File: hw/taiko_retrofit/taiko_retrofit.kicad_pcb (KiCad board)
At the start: 2 copper layers, 50 x 36 mm, 12 parts, among them J1 Conn_01x02, J2 Conn_01x03, J3 Conn_01x04, J4 Conn_01x02, U1 RP2040-Zero

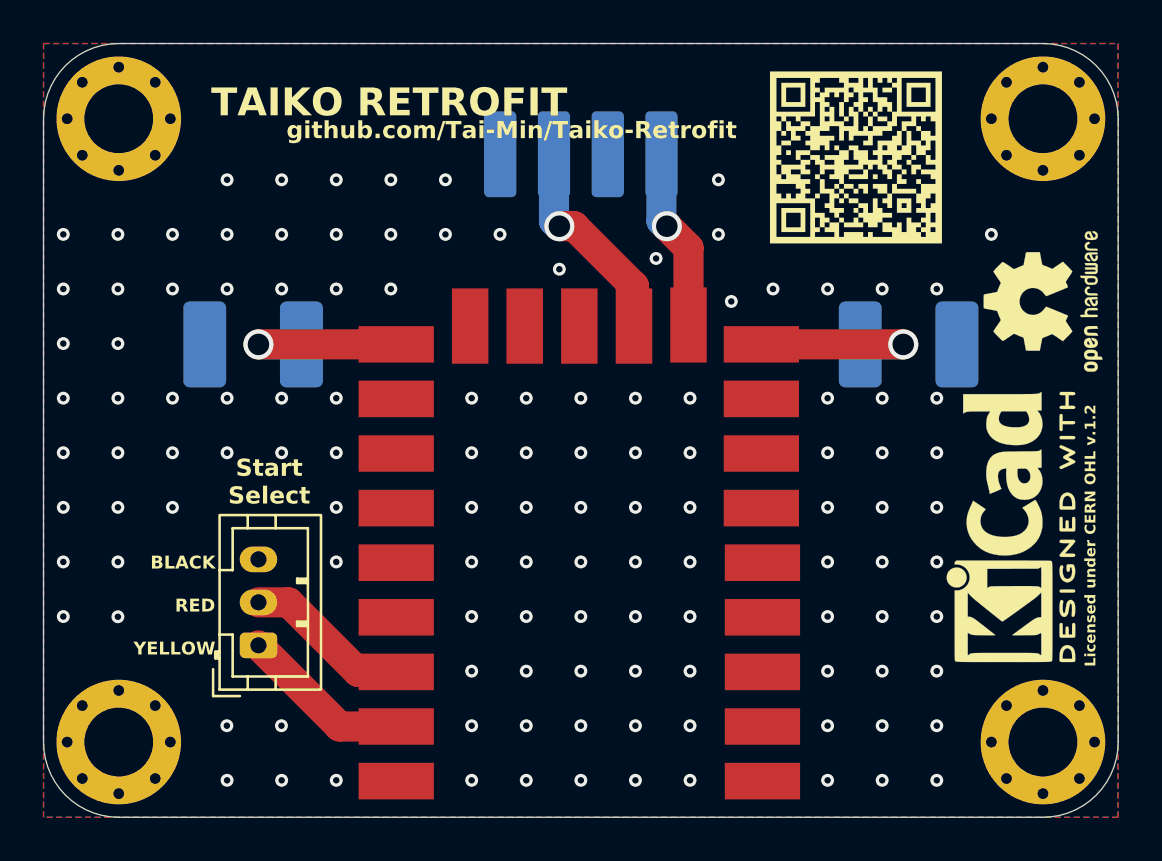
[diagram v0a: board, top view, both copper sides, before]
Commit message: Update PCB layout, add thanks README
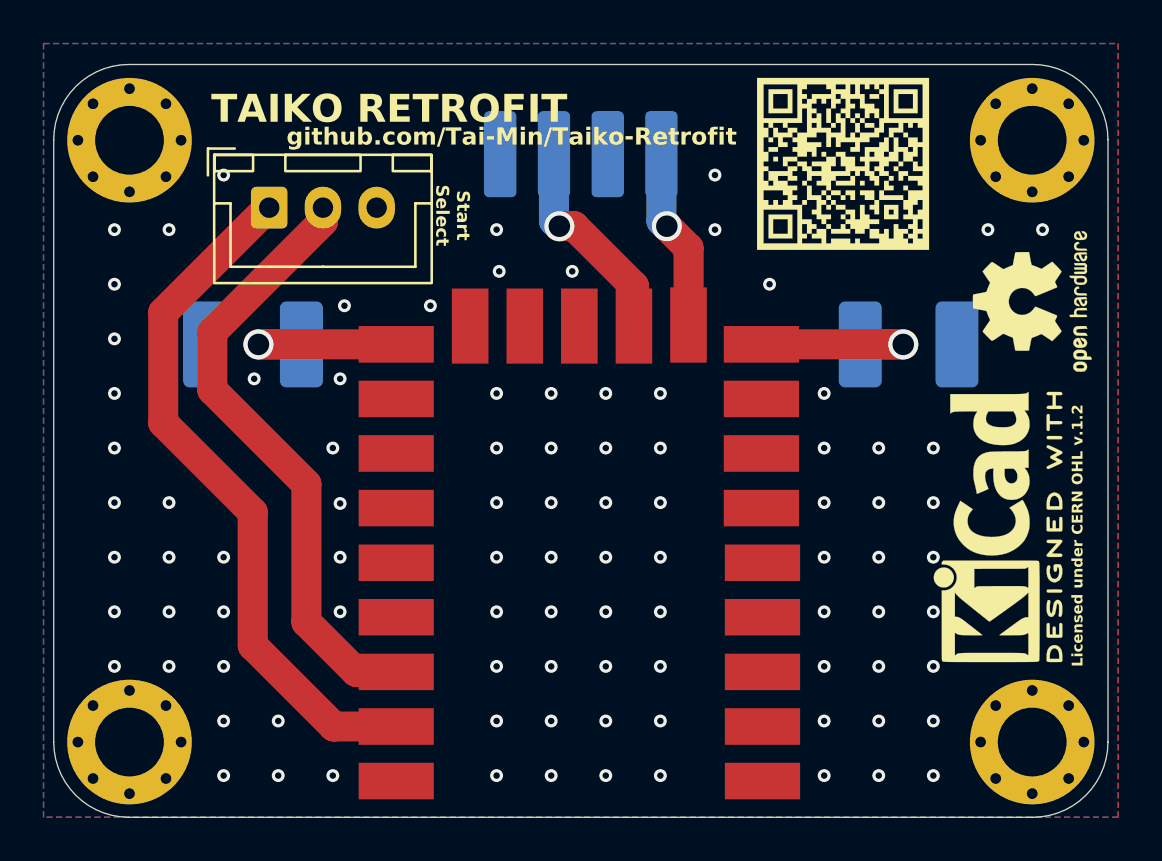
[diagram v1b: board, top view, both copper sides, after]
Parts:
- J2: footprint Connector_JST:JST_PH_B3B-PH-K_1x03_P2.00mm_Vertical -> Connector_JST:JST_XH_B3B-XH-A_1x03_P2.50mm_Vertical
- U1: footprint 3rdparty:RP2040 Zero -> RP2040-Zero:RP2040 Zero
- moved J2 20.4 mm to (133.0, 85.6), turned to 0 degrees
- moved H3 1.12 mm to (126.5, 82.5)
- moved H4 1.12 mm to (168.5, 82.5)
- moved G*** 0.67 mm to (159.7, 83.6)
- moved REF** 0.60 mm to (166.9, 100.5)
- moved H1 0.50 mm to (126.5, 110.5)
- moved H2 0.50 mm to (168.5, 110.5)
- moved REF** 0.50 mm to (168.5, 90.0)
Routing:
- net /START: track 7.97 -> 32.4 mm
- net /SELECT: track 7.75 -> 28.4 mm
- net GND: vias 123 -> 93
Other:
- board size 50 x 36 mm -> 49.1 x 35 mm
